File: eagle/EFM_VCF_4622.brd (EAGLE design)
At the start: 101.6 x 80.8 mm, 57 parts, among them IC1 LM13700N, Q1 2N3906, Q10 2N3904, Q11 2N3904, Q12 2N3904, Q13 2N3904, Q2 2N3904, Q3 2N3904, Q4 2N3904, Q5 2N3904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

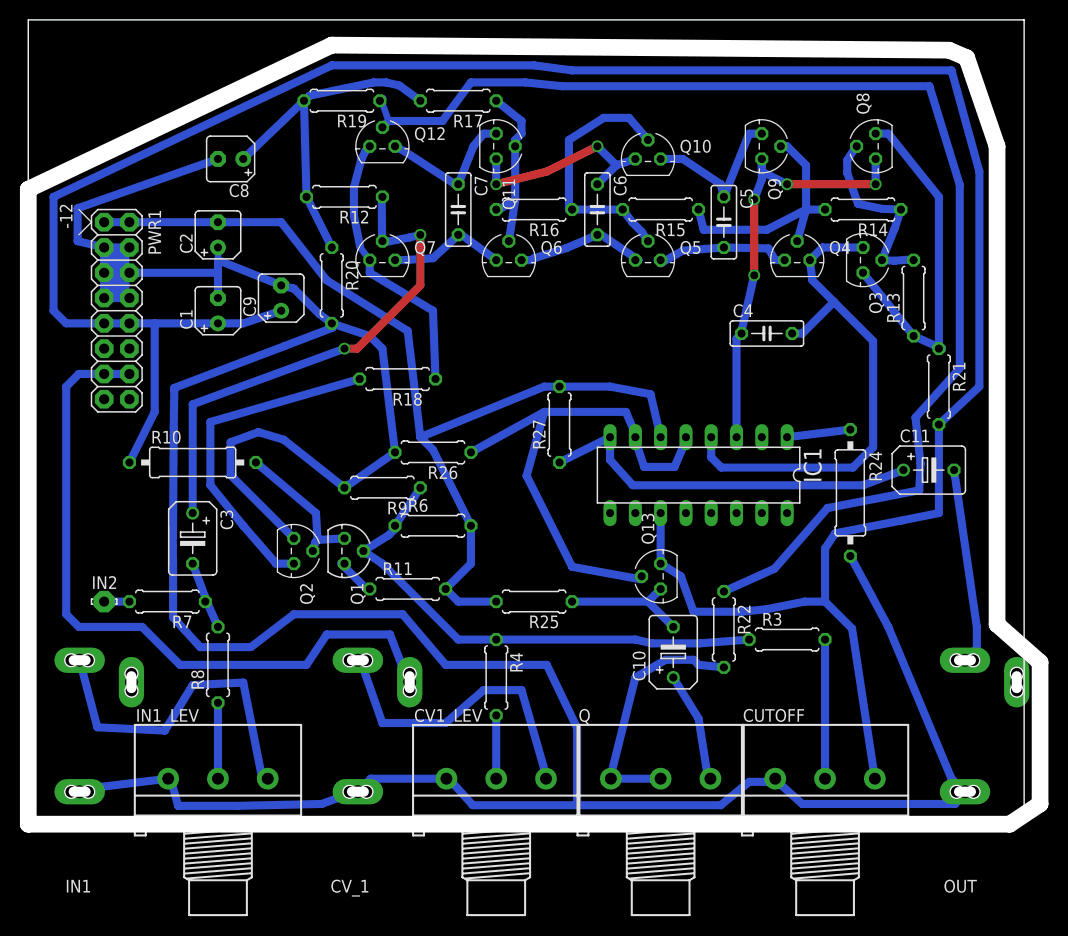
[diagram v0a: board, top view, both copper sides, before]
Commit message: neater layout and more cv and audio ins
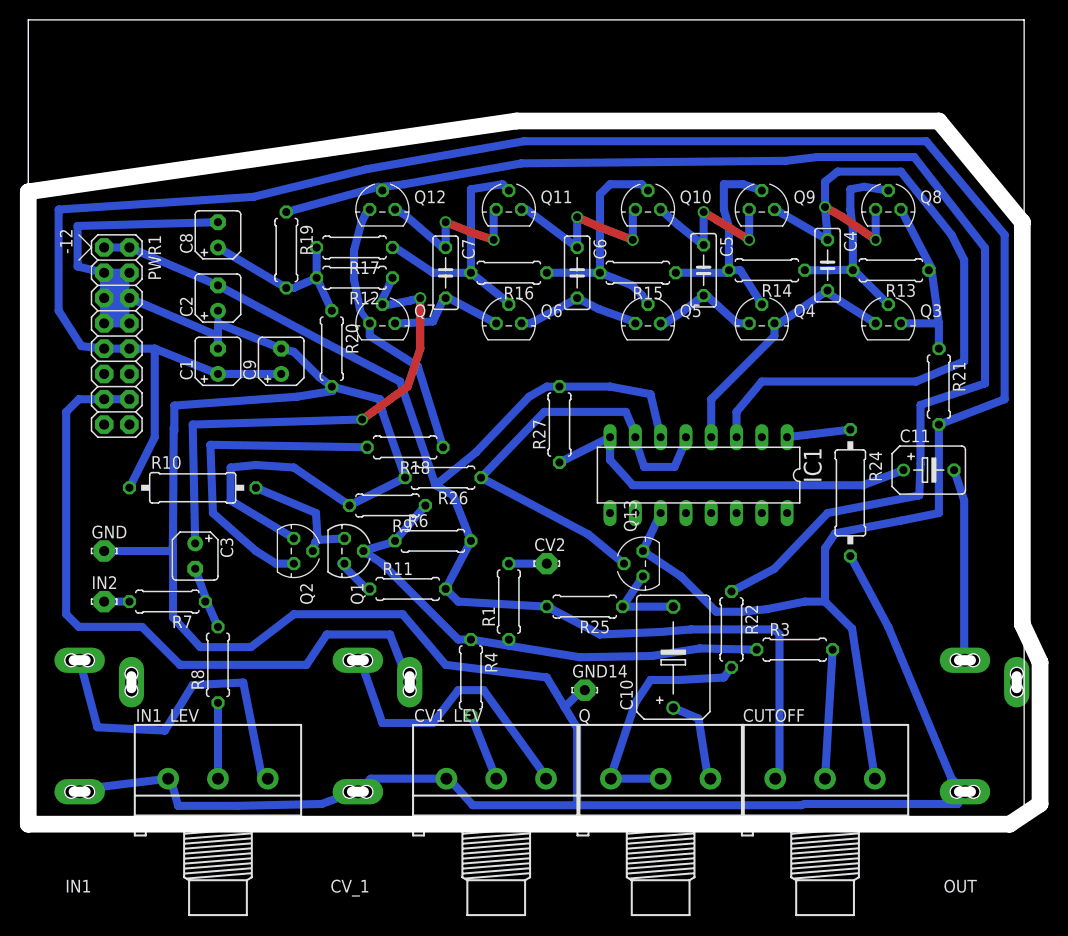
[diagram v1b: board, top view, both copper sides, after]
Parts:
- added CV2, GND, GND14: LSP10, solpad:LSP10
- added R1: 100k, rcl:0207/7
- C10: device rcl:B45181B -> rcl:B45181C
- C3: device rcl:B45181B -> rcl:B45181A
- moved R17 18.0 mm to (32.8, 57.1)
- moved R19 16.0 mm to (25.9, 56.9), turned to 270 degrees
- moved R14 11.4 mm to (74.2, 54.9)
- moved C4 9.18 mm to (80.3, 55.4), turned to 270 degrees
- moved R12 8.19 mm to (32.8, 54.1)
- moved C8 7.73 mm to (19.1, 58.4), turned to 90 degrees
- moved Q4 7.28 mm to (73.7, 49.5)
- moved R18 6.90 mm to (37.8, 37.1)
- moved Q3 6.84 mm to (86.4, 49.5), turned to 0 degrees
- moved R16 6.84 mm to (48.3, 54.6)
- moved R15 6.75 mm to (61.2, 54.6)
- moved C6 6.67 mm to (55.1, 54.6)
- moved C7 6.48 mm to (41.9, 54.6)
- moved Q11 6.48 mm to (48.3, 61.0), turned to 0 degrees
- moved Q8 6.48 mm to (86.4, 61.0), turned to 0 degrees
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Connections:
- new net N$11: CV2.MP, R1.2
- net -12V: now also CUTOFF.1
- net GND: now also GND.MP, GND14.MP; no longer CUTOFF.1
- net N$20: now also R1.1
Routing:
- net -12V: track 97.5 -> 137.0 mm
- net N$12: track 44.0 -> 77.5 mm, vias 4 -> 2
- net N$9: track 52.3 -> 26.4 mm
- net N$25: track 36.3 -> 17.9 mm
- net N$43: track 36.1 -> 19.1 mm
- net N$50: track 17.8 -> 26.1 mm
- net +12V: track 250.7 -> 243.7 mm
- net N$19: track 53.0 -> 46.3 mm
- net N$35: track 13.0 -> 8.74 mm
- net N$11: track 0.00 -> 3.81 mm
- net N$17: track 14.5 -> 17.3 mm, vias 0 -> 2
- net N$46: track 25.9 -> 23.3 mm
- net N$44: track 19.4 -> 21.9 mm
- net N$55: track 73.7 -> 71.2 mm
- net N$14: track 14.2 -> 11.7 mm
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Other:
- outline, holes or cut-outs redrawn

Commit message: tidied still more
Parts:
- R10: device rcl:0309/12 -> rcl:0309/10
- R24: device rcl:0309/12 -> rcl:0207/7
- moved Q13 8.98 mm to (52.8, 26.7)
- moved CV2 6.67 mm to (45.7, 27.4)
- moved C4 3.81 mm to (80.3, 51.6)
- moved C6 3.81 mm to (55.1, 50.8)
- moved C7 3.81 mm to (41.9, 50.8)
- moved Q10 3.81 mm to (62.2, 57.1)
- moved Q11 3.81 mm to (48.3, 57.1)
- moved Q12 3.81 mm to (35.6, 57.1)
- moved Q3 3.81 mm to (86.4, 45.7)
- moved Q4 3.81 mm to (73.7, 45.7)
- moved Q5 3.81 mm to (62.2, 45.7)
- moved Q6 3.81 mm to (48.3, 45.7)
- moved Q7 3.81 mm to (35.6, 45.7)
- moved Q8 3.81 mm to (86.4, 57.1)
- moved Q9 3.81 mm to (73.7, 57.1)
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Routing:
- net N$19: track 46.3 -> 36.0 mm
- net GND: track 328.1 -> 321.0 mm
- net N$35: track 8.74 -> 14.0 mm
- net N$55: track 71.2 -> 66.8 mm
- net -12V: track 137.0 -> 132.7 mm
- net +12V: track 243.7 -> 247.9 mm
- net N$7: track 51.0 -> 47.5 mm
- net N$31: track 19.5 -> 16.0 mm
- net N$27: track 4.23 -> 5.46 mm
- net N$25: track 17.9 -> 16.7 mm
- net N$1: track 6.40 -> 7.58 mm
- net N$3: track 32.5 -> 31.6 mm
- net N$44: track 21.9 -> 21.1 mm
- net N$4: track 27.7 -> 27.1 mm
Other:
- outline, holes or cut-outs redrawn
